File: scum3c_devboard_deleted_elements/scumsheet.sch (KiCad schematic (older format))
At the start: 16 parts, among them U8 scum3

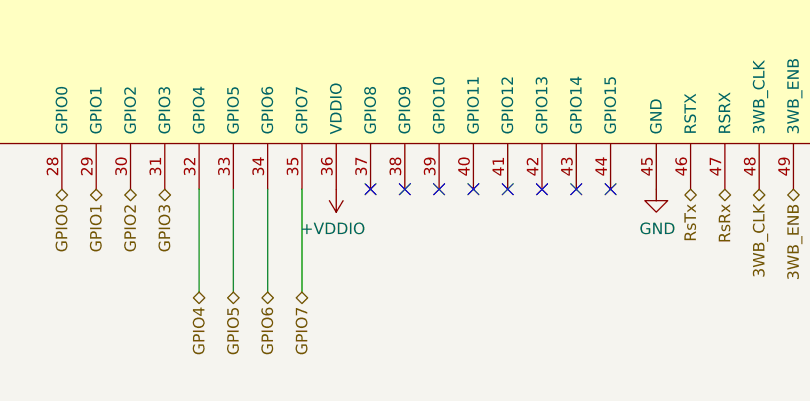
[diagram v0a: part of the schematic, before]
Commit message: added gpio 8 9 10 and gnd pins
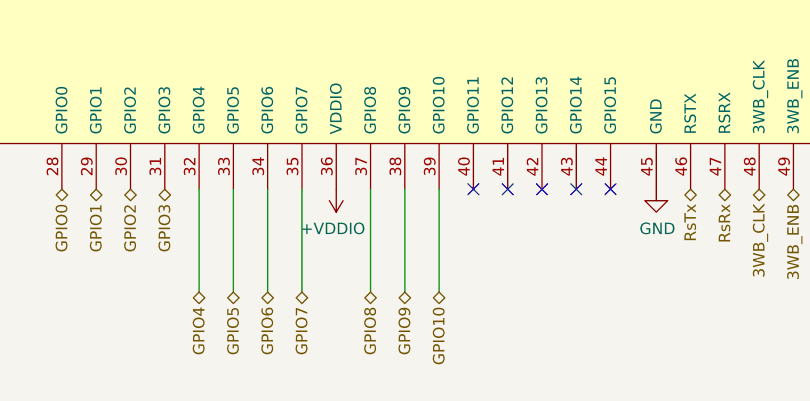
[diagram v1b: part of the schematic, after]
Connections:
- net GPIO8: now reaches U8.37 (GPIO8)
- net GPIO9: now reaches U8.38 (GPIO9)
- net GPIO10: now reaches U8.39 (GPIO10)
- no-connect marks 59 -> 56
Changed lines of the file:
@@
 NoConn ~ 5650 6050
 NoConn ~ 5500 6050
-NoConn ~ 5350 6050
-NoConn ~ 5200 6050
-NoConn ~ 5050 6050
 Text HLabel 8000 5100 2    50   BiDi ~ 0
 SENSOR_EXT_IN
 Text HLabel 8000 5250 2    50   BiDi ~ 0
 SENSOR_LDO_OUTPUT
+Text HLabel 5050 6500 3    50   BiDi ~ 0
+GPIO8
+Wire Wire Line
+	5050 6500 5050 6050
+Text HLabel 5200 6500 3    50   BiDi ~ 0
+GPIO9
+Wire Wire Line
+	5200 6500 5200 6050
+Text HLabel 5350 6500 3    50   BiDi ~ 0
+GPIO10
+Wire Wire Line
+	5350 6500 5350 6050
 $EndSCHEMATC

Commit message: added gpio8-10
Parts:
- U8: footprint SCUM:QFN-100_EP_12x12_Pitch0.4mm_Margin0.25mm -> SCUM:QFN-100_EP_12x12_Pitch0.4_mm_redo
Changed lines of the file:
@@
 F 0 "U8" H 8944 3271 50  0000 L CNN
 F 1 "scum3" H 8944 3180 50  0000 L CNN
-F 2 "SCUM:QFN-100_EP_12x12_Pitch0.4mm_Margin0.25mm" H 5200 3450 50  0001 C CNN
+F 2 "SCUM:QFN-100_EP_12x12_Pitch0.4_mm_redo" H 5200 3450 50  0001 C CNN
 F 3 "" H 5200 3450 50  0001 C CNN
 	1    5200 3450

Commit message: Revert "added gpio8-10"
This reverts commit daf7284f57cd8196d10e3621e3573955ecb68719.
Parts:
- U8: footprint SCUM:QFN-100_EP_12x12_Pitch0.4_mm_redo -> SCUM:QFN-100_EP_12x12_Pitch0.4mm_Margin0.25mm
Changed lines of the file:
@@
 F 0 "U8" H 8944 3271 50  0000 L CNN
 F 1 "scum3" H 8944 3180 50  0000 L CNN
-F 2 "SCUM:QFN-100_EP_12x12_Pitch0.4_mm_redo" H 5200 3450 50  0001 C CNN
+F 2 "SCUM:QFN-100_EP_12x12_Pitch0.4mm_Margin0.25mm" H 5200 3450 50  0001 C CNN
 F 3 "" H 5200 3450 50  0001 C CNN
 	1    5200 3450

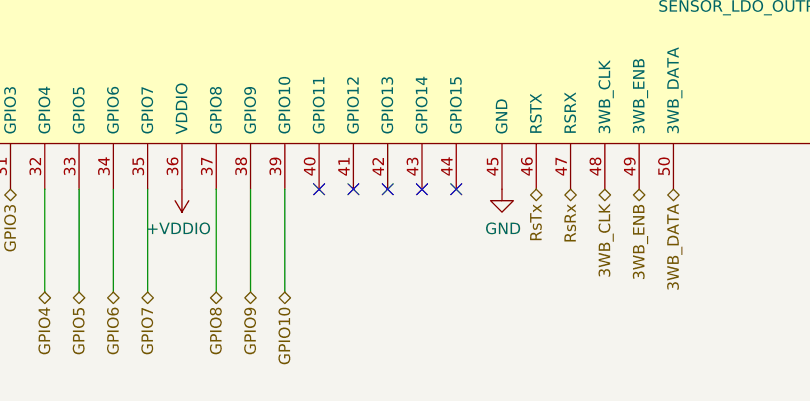
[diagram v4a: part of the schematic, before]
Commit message: connected IMU
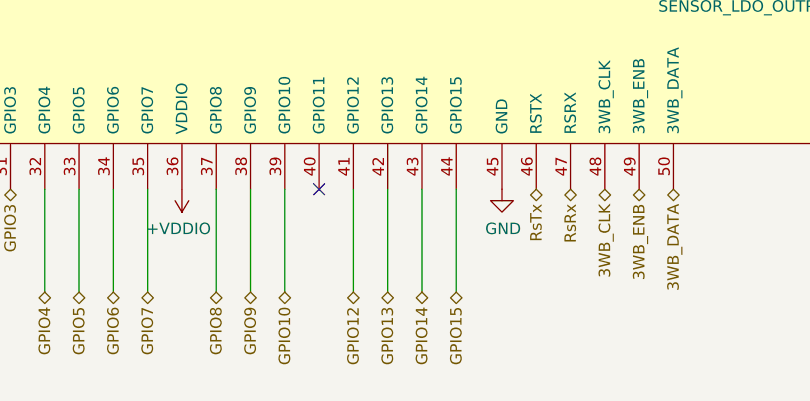
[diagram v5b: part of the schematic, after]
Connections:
- net GPIO12: now reaches U8.41 (GPIO12)
- net GPIO13: now reaches U8.42 (GPIO13)
- net GPIO14: now reaches U8.43 (GPIO14)
- net GPIO15: now reaches U8.44 (GPIO15)
- no-connect marks 56 -> 52
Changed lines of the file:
@@
 $EndComp
 NoConn ~ 2250 4100
-NoConn ~ 6100 6050
-NoConn ~ 5950 6050
-NoConn ~ 5800 6050
-NoConn ~ 5650 6050
 NoConn ~ 5500 6050
 Text HLabel 8000 5100 2    50   BiDi ~ 0
@@
 	0    -1   -1   0
 $EndComp
+Text HLabel 5650 6500 3    50   BiDi ~ 0
+GPIO12
+Text HLabel 5800 6500 3    50   BiDi ~ 0
+GPIO13
+Text HLabel 5950 6500 3    50   BiDi ~ 0
+GPIO14
+Text HLabel 6100 6500 3    50   BiDi ~ 0
+GPIO15
+Wire Wire Line
+	5650 6050 5650 6500
+Wire Wire Line
+	5800 6050 5800 6500
+Wire Wire Line
+	5950 6050 5950 6500
+Wire Wire Line
+	6100 6050 6100 6500
 $EndSCHEMATC

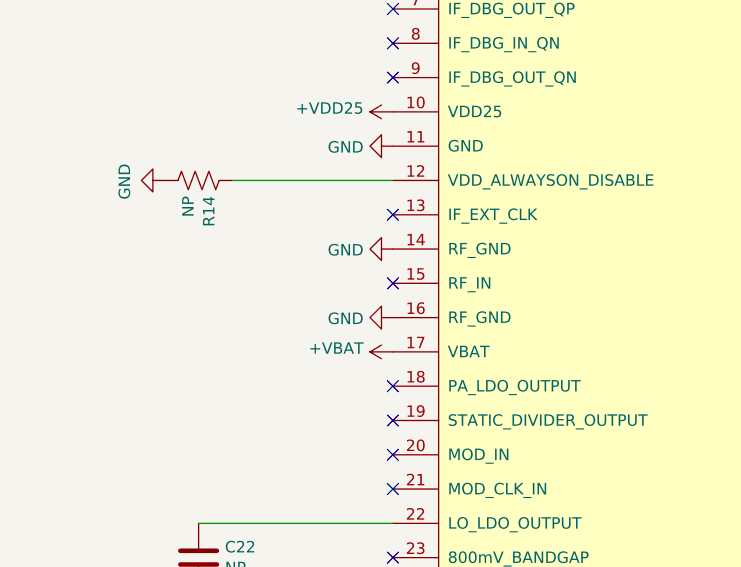
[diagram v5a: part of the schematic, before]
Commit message: Added antenna pin.
Also:
- added antenna pin to SCuM (not ideal, but it's there)
- increased screw hole size slightly for better M1.6 screw fit
- rounded board corners
- fixed part labels
- added name "McCoy" and logo
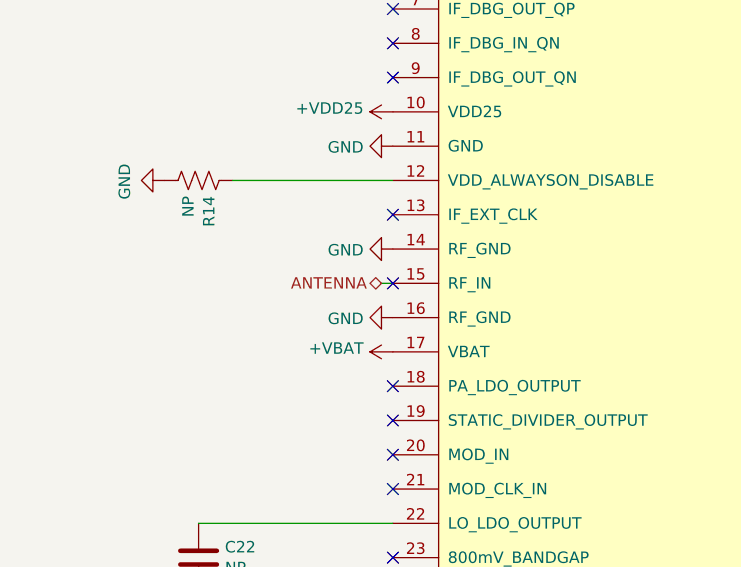
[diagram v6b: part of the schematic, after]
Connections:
- net ANTENNA: now reaches U8.15 (RF_IN)
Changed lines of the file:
@@
 EESchema Schematic File Version 4
+LIBS:scum3c-devboard-cache
 EELAYER 30 0
 EELAYER END
@@
 	1    0    0    -1
 $EndComp
-Wire Wire Line
-	2250 5150 1400 5150
 $Comp
 L draft1library:+VBAT #PWR0176
@@
 	1    0    0    -1
 $EndComp
-Wire Wire Line
-	2250 3650 1550 3650
 $Comp
 L draft1library:+VBAT #PWR0193
@@
 	0    -1   -1   0
 $EndComp
+NoConn ~ 5500 6050
+Text HLabel 8000 5100 2    50   BiDi ~ 0
+SENSOR_EXT_IN
+Text HLabel 8000 5250 2    50   BiDi ~ 0
+SENSOR_LDO_OUTPUT
+Text HLabel 5050 6500 3    50   BiDi ~ 0
+GPIO8
+Wire Wire Line
+	5050 6500 5050 6050
+Text HLabel 5200 6500 3    50   BiDi ~ 0
+GPIO9
+Wire Wire Line
+	5200 6500 5200 6050
+Text HLabel 5350 6500 3    50   BiDi ~ 0
+GPIO10
+Wire Wire Line
+	5350 6500 5350 6050
+$Comp
+L power:GND #PWR0190
+U 1 1 5F3FB8E1
+P 800 2450
+AR Path="/5F3B1D81/5F3FB8E1" Ref="#PWR0190"  Part="1"
+AR Path="/5F41418C/5F3FB8E1" Ref="#PWR?"  Part="1"
+AR Path="/5F414989/5F3FB8E1" Ref="#PWR?"  Part="1"
+F 0 "#PWR0190" H 800 2200 50  0001 C CNN
+F 1 "GND" H 805 2277 50  0000 C CNN
+F 2 "" H 800 2450 50  0001 C CNN
+F 3 "" H 800 2450 50  0001 C CNN
+	1    800  2450
+	1    0    0    -1
+$EndComp
+$Comp
+L draft1library:+VDD25 #PWR0188
+U 1 1 5F3F91ED
+P 800 2150
+AR Path="/5F3B1D81/5F3F91ED" Ref="#PWR0188"  Part="1"
+AR Path="/5F41418C/5F3F91ED" Ref="#PWR?"  Part="1"
+AR Path="/5F414989/5F3F91ED" Ref="#PWR?"  Part="1"
+F 0 "#PWR0188" H 800 2000 50  0001 C CNN
+F 1 "+VDD25" H 815 2323 50  0000 C CNN
+F 2 "" H 800 2150 50  0001 C CNN
+F 3 "" H 800 2150 50  0001 C CNN
+	1    800  2150
+	1    0    0    -1
+$EndComp
+$Comp
+L Device:C C21
+U 1 1 5F3FABA5
+P 800 2300
+AR Path="/5F3B1D81/5F3FABA5" Ref="C21"  Part="1"
+AR Path="/5F41418C/5F3FABA5" Ref="C?"  Part="1"
+AR Path="/5F414989/5F3FABA5" Ref="C?"  Part="1"
+F 0 "C21" H 915 2346 50  0000 L CNN
+F 1 "NP" H 915 2255 50  0000 L CNN
+F 2 "Capacitor_SMD:C_0402_1005Metric" H 838 2150 50  0001 C CNN
+F 3 "~" H 800 2300 50  0001 C CNN
+	1    800  2300
+	1    0    0    -1
+$EndComp
+$Comp
+L draft1library:+VDD25 #PWR0192
+U 1 1 5F3FC7C2
+P 2250 3350
+AR Path="/5F3B1D81/5F3FC7C2" Ref="#PWR0192"  Part="1"
+AR Path="/5F41418C/5F3FC7C2" Ref="#PWR?"  Part="1"
+AR Path="/5F414989/5F3FC7C2" Ref="#PWR?"  Part="1"
+F 0 "#PWR0192" H 2250 3200 50  0001 C CNN
+F 1 "+VDD25" V 2265 3478 50  0000 L CNN
+F 2 "" H 2250 3350 50  0001 C CNN
+F 3 "" H 2250 3350 50  0001 C CNN
+	1    2250 3350
+	0    -1   -1   0
+$EndComp
+Text HLabel 5650 6500 3    50   BiDi ~ 0
+GPIO12
+Text HLabel 5800 6500 3    50   BiDi ~ 0
+GPIO13
+Text HLabel 5950 6500 3    50   BiDi ~ 0
+GPIO14
+Text HLabel 6100 6500 3    50   BiDi ~ 0
+GPIO15
+Wire Wire Line
+	5650 6050 5650 6500
+Wire Wire Line
+	5800 6050 5800 6500
+Wire Wire Line
+	5950 6050 5950 6500
+Wire Wire Line
+	6100 6050 6100 6500
+Wire Wire Line
+	2250 5150 1400 5150
+Wire Wire Line
+	2250 3650 1550 3650
+NoConn ~ 2250 4100
 $Comp
 L draft1library:scum3 U8
@@
 	1    0    0    -1
 $EndComp
-NoConn ~ 2250 4100
-NoConn ~ 5500 6050
-Text HLabel 8000 5100 2    50   BiDi ~ 0
-SENSOR_EXT_IN
-Text HLabel 8000 5250 2    50   BiDi ~ 0
-SENSOR_LDO_OUTPUT
-Text HLabel 5050 6500 3    50   BiDi ~ 0
-GPIO8
-Wire Wire Line
-	5050 6500 5050 6050
-Text HLabel 5200 6500 3    50   BiDi ~ 0
-GPIO9
-Wire Wire Line
-	5200 6500 5200 6050
-Text HLabel 5350 6500 3    50   BiDi ~ 0
-GPIO10
-Wire Wire Line
-	5350 6500 5350 6050
-$Comp
-L power:GND #PWR0190
-U 1 1 5F3FB8E1
-P 800 2450
-AR Path="/5F3B1D81/5F3FB8E1" Ref="#PWR0190"  Part="1"
-AR Path="/5F41418C/5F3FB8E1" Ref="#PWR?"  Part="1"
-AR Path="/5F414989/5F3FB8E1" Ref="#PWR?"  Part="1"
-F 0 "#PWR0190" H 800 2200 50  0001 C CNN
-F 1 "GND" H 805 2277 50  0000 C CNN
-F 2 "" H 800 2450 50  0001 C CNN
-F 3 "" H 800 2450 50  0001 C CNN
-	1    800  2450
-	1    0    0    -1
-$EndComp
-$Comp
-L draft1library:+VDD25 #PWR0188
-U 1 1 5F3F91ED
-P 800 2150
-AR Path="/5F3B1D81/5F3F91ED" Ref="#PWR0188"  Part="1"
-AR Path="/5F41418C/5F3F91ED" Ref="#PWR?"  Part="1"
-AR Path="/5F414989/5F3F91ED" Ref="#PWR?"  Part="1"
-F 0 "#PWR0188" H 800 2000 50  0001 C CNN
-F 1 "+VDD25" H 815 2323 50  0000 C CNN
-F 2 "" H 800 2150 50  0001 C CNN
-F 3 "" H 800 2150 50  0001 C CNN
-	1    800  2150
-	1    0    0    -1
-$EndComp
-$Comp
-L Device:C C21
-U 1 1 5F3FABA5
-P 800 2300
-AR Path="/5F3B1D81/5F3FABA5" Ref="C21"  Part="1"
-AR Path="/5F41418C/5F3FABA5" Ref="C?"  Part="1"
-AR Path="/5F414989/5F3FABA5" Ref="C?"  Part="1"
-F 0 "C21" H 915 2346 50  0000 L CNN
-F 1 "NP" H 915 2255 50  0000 L CNN
-F 2 "Capacitor_SMD:C_0402_1005Metric" H 838 2150 50  0001 C CNN
-F 3 "~" H 800 2300 50  0001 C CNN
-	1    800  2300
-	1    0    0    -1
-$EndComp
-$Comp
-L draft1library:+VDD25 #PWR0192
-U 1 1 5F3FC7C2
-P 2250 3350
-AR Path="/5F3B1D81/5F3FC7C2" Ref="#PWR0192"  Part="1"
-AR Path="/5F41418C/5F3FC7C2" Ref="#PWR?"  Part="1"
-AR Path="/5F414989/5F3FC7C2" Ref="#PWR?"  Part="1"
-F 0 "#PWR0192" H 2250 3200 50  0001 C CNN
-F 1 "+VDD25" V 2265 3478 50  0000 L CNN
-F 2 "" H 2250 3350 50  0001 C CNN
-F 3 "" H 2250 3350 50  0001 C CNN
-	1    2250 3350
-	0    -1   -1   0
-$EndComp
-Text HLabel 5650 6500 3    50   BiDi ~ 0
-GPIO12
-Text HLabel 5800 6500 3    50   BiDi ~ 0
-GPIO13
-Text HLabel 5950 6500 3    50   BiDi ~ 0
-GPIO14
-Text HLabel 6100 6500 3    50   BiDi ~ 0
-GPIO15
-Wire Wire Line
-	5650 6050 5650 6500
-Wire Wire Line
-	5800 6050 5800 6500
-Wire Wire Line
-	5950 6050 5950 6500
-Wire Wire Line
-	6100 6050 6100 6500
+Text HLabel 2200 4100 0    50   BiDi ~ 0
+ANTENNA
+Wire Wire Line
+	2200 4100 2250 4100
 $EndSCHEMATC

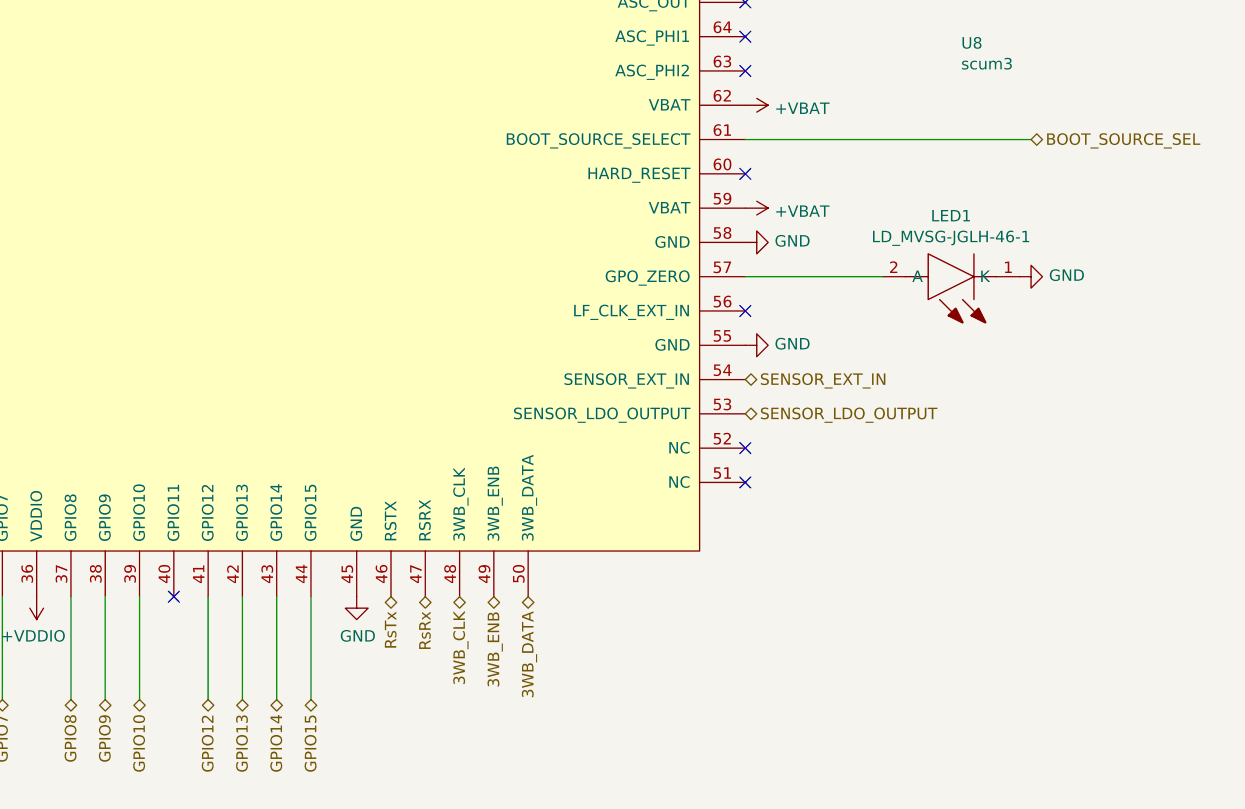
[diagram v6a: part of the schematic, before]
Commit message: placed gpio traces
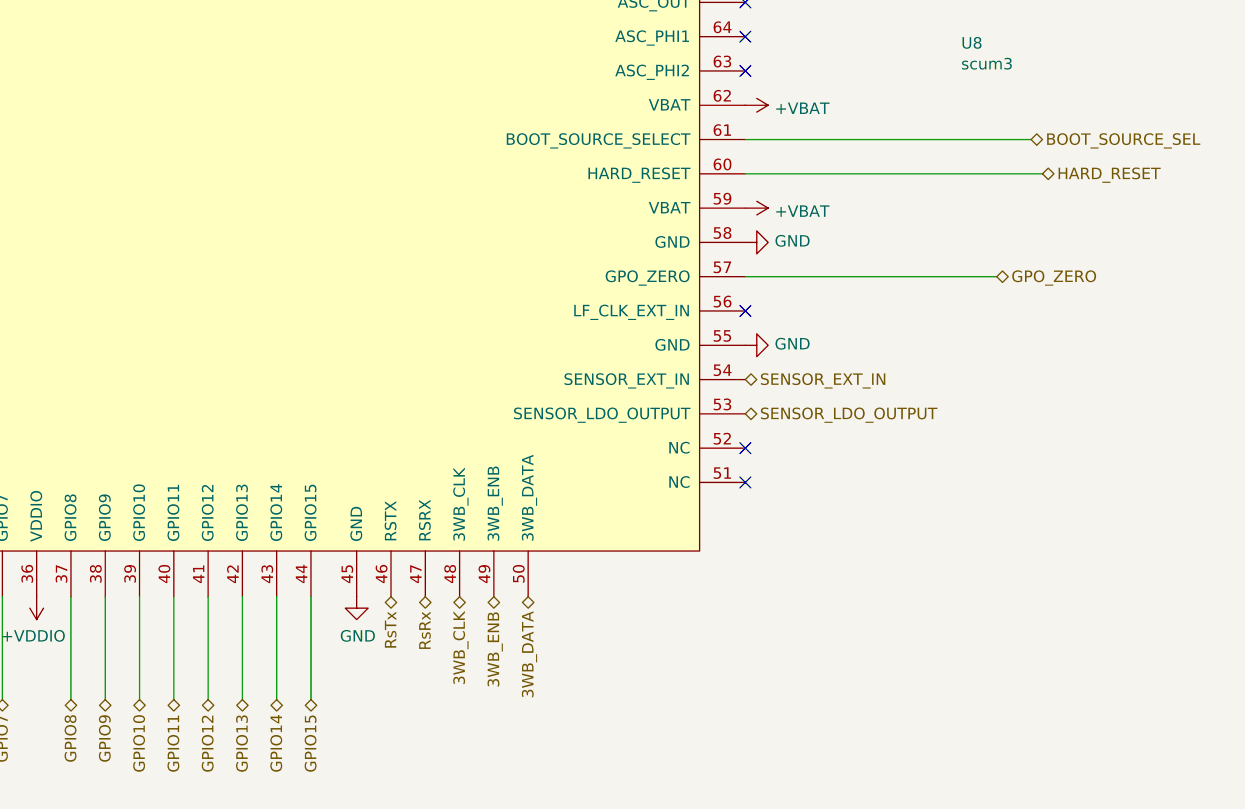
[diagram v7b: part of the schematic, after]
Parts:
- removed LED1: LD_MVSG-JGLH-46-1, SamacSys_Parts:LEDM2218X140N, symbol SamacSys_Parts:LD_MVSG-JGLH-46-1
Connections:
- net GPIO11: now reaches U8.40 (GPIO11)
- net GPO_ZERO: now reaches U8.57 (GPO_ZERO)
- net HARD_RESET: now reaches U8.60 (HARD_RESET)
- no-connect marks 52 -> 50
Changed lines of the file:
@@
 EESchema Schematic File Version 4
-LIBS:scum3c-devboard-cache
 EELAYER 30 0
 EELAYER END
@@
 NoConn ~ 8000 3750
 NoConn ~ 8000 4800
-NoConn ~ 8000 4200
 Wire Wire Line
 	8000 2550 9150 2550
@@
 Text HLabel 9250 4050 2    50   BiDi ~ 0
 BOOT_SOURCE_SEL
-$Comp
-L SamacSys_Parts:LD_MVSG-JGLH-46-1 LED1
-U 1 1 5F7B4972
-P 9200 4650
-F 0 "LED1" H 9500 4385 50  0000 C CNN
-F 1 "LD_MVSG-JGLH-46-1" H 9500 4476 50  0000 C CNN
-F 2 "SamacSys_Parts:LEDM2218X140N" H 9700 4800 50  0001 L BNN
-F 3 "https://dammedia.osram.info/media/resource/hires/osram-dam-6917470/LD%20MVSG_EN.pdf" H 9700 4700 50  0001 L BNN
-F 4 "Osram Opto LD MVSG-JGLH-46-1, Mini TOPLED Series Blue LED, 465 nm,, Rectangle Lens SMD Package" H 9700 4600 50  0001 L BNN "Description"
-F 5 "1.4" H 9700 4500 50  0001 L BNN "Height"
-F 6 "OSRAM" H 9700 4400 50  0001 L BNN "Manufacturer_Name"
-F 7 "LD MVSG-JGLH-46-1" H 9700 4300 50  0001 L BNN "Manufacturer_Part_Number"
-F 8 "LD MVSG-JGLH-46-1" H 9700 4200 50  0001 L BNN "Arrow Part Number"
-F 9 "https://www.arrow.com/en/products/ldmvsg-jglh-46-1/osram-opto-semiconductors" H 9700 4100 50  0001 L BNN "Arrow Price/Stock"
-F 10 "720-LDMVSGJGLH461" H 9700 4000 50  0001 L BNN "Mouser Part Number"
-F 11 "https://www.mouser.co.uk/ProductDetail/OSRAM-Opto-Semiconductors/LD-MVSG-JGLH-46-1?qs=znB0%2F8lYn%252BuYpqaPHtqGHw%3D%3D" H 9700 3900 50  0001 L BNN "Mouser Price/Stock"
-	1    9200 4650
-	-1   0    0    1
-$EndComp
-Wire Wire Line
-	8000 4650 8600 4650
-$Comp
-L power:GND #PWR0125
-U 1 1 5F7B7D3D
-P 9200 4650
-F 0 "#PWR0125" H 9200 4400 50  0001 C CNN
-F 1 "GND" V 9205 4522 50  0000 R CNN
-F 2 "" H 9200 4650 50  0001 C CNN
-F 3 "" H 9200 4650 50  0001 C CNN
-	1    9200 4650
-	0    -1   -1   0
-$EndComp
-NoConn ~ 5500 6050
 Text HLabel 8000 5100 2    50   BiDi ~ 0
 SENSOR_EXT_IN
@@
 Wire Wire Line
 	2200 4100 2250 4100
+Wire Wire Line
+	8000 4200 9300 4200
+Text HLabel 9300 4200 2    50   BiDi ~ 0
+HARD_RESET
+Text HLabel 5500 6500 3    50   BiDi ~ 0
+GPIO11
+Wire Wire Line
+	5500 6050 5500 6500
+Wire Wire Line
+	8000 4650 9100 4650
+Text HLabel 9100 4650 2    50   BiDi ~ 0
+GPO_ZERO
 $EndSCHEMATC
